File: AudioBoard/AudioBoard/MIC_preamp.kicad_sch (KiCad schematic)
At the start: 31 parts, among them SW1 SW_SPDT, U2 NE5532, U3 NE5532

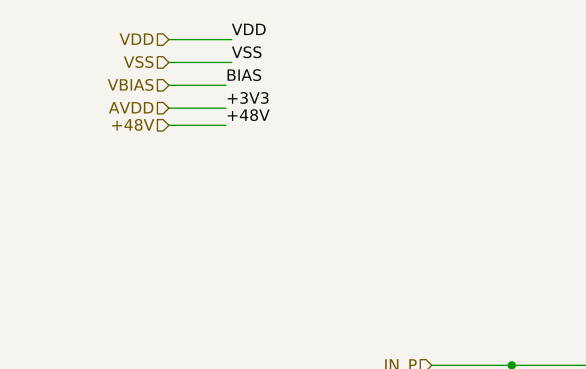
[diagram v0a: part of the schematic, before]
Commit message: added xlr output stage
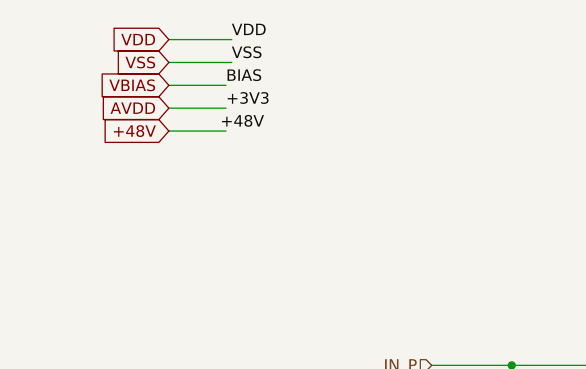
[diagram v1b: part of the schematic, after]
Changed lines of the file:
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@@
 	(wire
 		(pts
-			(xy 39.37 27.305) (xy 45.72 27.305)
+			(xy 39.37 27.94) (xy 45.72 27.94)
 		)
 		(stroke
@@
 	)
 	(label "+48V"
-		(at 45.72 27.305 0)
+		(at 45.085 27.94 0)
 		(effects
 			(font
@@
 			)
 			(justify right bottom)
+		)
+	)
+	(global_label "AVDD"
+		(shape input)
+		(at 39.37 25.4 180)
+		(fields_autoplaced yes)
+		(effects
+			(font
+				(size 1.27 1.27)
+			)
+			(justify right)
+		)
+		(property "Intersheetrefs" "${INTERSHEET_REFS}"
+			(at 31.6676 25.4 0)
+			(hide yes)
+			(show_name no)
+			(do_not_autoplace no)
+			(effects
+				(font
+					(size 1.27 1.27)
+				)
+				(justify right)
+			)
+		)
+	)
+	(global_label "VSS"
+		(shape input)
+		(at 39.37 20.32 180)
+		(fields_autoplaced yes)
+		(effects
+			(font
+				(size 1.27 1.27)
+			)
+			(justify right)
+		)
+		(property "Intersheetrefs" "${INTERSHEET_REFS}"
+			(at 32.8772 20.32 0)
+			(hide yes)
+			(show_name no)
+			(do_not_autoplace no)
+			(effects
+				(font
+					(size 1.27 1.27)
+				)
+				(justify right)
+			)
+		)
+	)
+	(global_label "+48V"
+		(shape input)
+		(at 39.37 27.94 180)
+		(fields_autoplaced yes)
+		(effects
+			(font
+				(size 1.27 1.27)
+			)
+			(justify right)
+		)
+		(property "Intersheetrefs" "${INTERSHEET_REFS}"
+			(at 31.3048 27.94 0)
+			(hide yes)
+			(show_name no)
+			(do_not_autoplace no)
+			(effects
+				(font
+					(size 1.27 1.27)
+				)
+				(justify right)
+			)
+		)
+	)
+	(global_label "VBIAS"
+		(shape input)
+		(at 39.37 22.86 180)
+		(fields_autoplaced yes)
+		(effects
+			(font
+				(size 1.27 1.27)
+			)
+			(justify right)
+		)
+		(property "Intersheetrefs" "${INTERSHEET_REFS}"
+			(at 31.1233 22.86 0)
+			(hide yes)
+			(show_name no)
+			(do_not_autoplace no)
+			(effects
+				(font
+					(size 1.27 1.27)
+				)
+				(justify right)
+			)
+		)
+	)
+	(global_label "VDD"
+		(shape input)
+		(at 39.37 17.78 180)
+		(fields_autoplaced yes)
+		(effects
+			(font
+				(size 1.27 1.27)
+			)
+			(justify right)
+		)
+		(property "Intersheetrefs" "${INTERSHEET_REFS}"
+			(at 32.7562 17.78 0)
+			(hide yes)
+			(show_name no)
+			(do_not_autoplace no)
+			(effects
+				(font
+					(size 1.27 1.27)
+				)
+				(justify right)
+			)
 		)
 	)
@@
 		)
 	)
-	(hierarchical_label "VSS"
-		(shape input)
-		(at 39.37 20.32 180)
-		(effects
-			(font
-				(size 1.27 1.27)
-			)
-			(justify right)
-		)
-	)
-	(hierarchical_label "VBIAS"
-		(shape input)
-		(at 39.37 22.86 180)
-		(effects
-			(font
-				(size 1.27 1.27)
-			)
-			(justify right)
-		)
-	)
-	(hierarchical_label "AVDD"
-		(shape input)
-		(at 39.37 25.4 180)
-		(effects
-			(font
-				(size 1.27 1.27)
-			)
-			(justify right)
-		)
-	)
-	(hierarchical_label "VDD"
-		(shape input)
-		(at 39.37 17.78 180)
-		(effects
-			(font
-				(size 1.27 1.27)
-			)
-			(justify right)
-		)
-	)
 	(hierarchical_label "OUT_P"
 		(shape output)
@@
 		)
 	)
-	(hierarchical_label "+48V"
-		(shape input)
-		(at 39.37 27.305 180)
-		(effects
-			(font
-				(size 1.27 1.27)
-			)
-			(justify right)
-		)
-	)

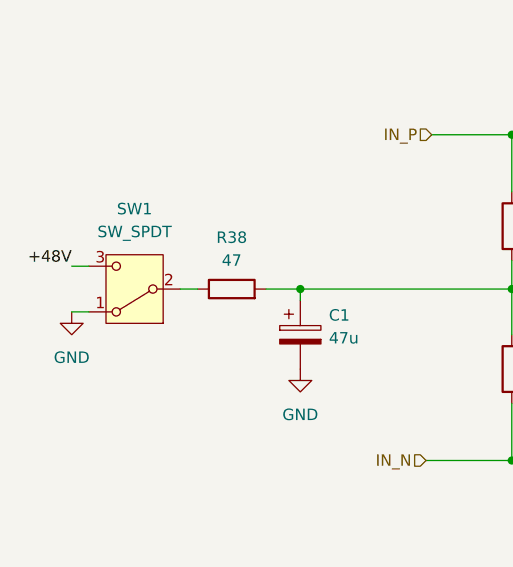
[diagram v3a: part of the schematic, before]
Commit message: added lcscpart to components and assigned footprints
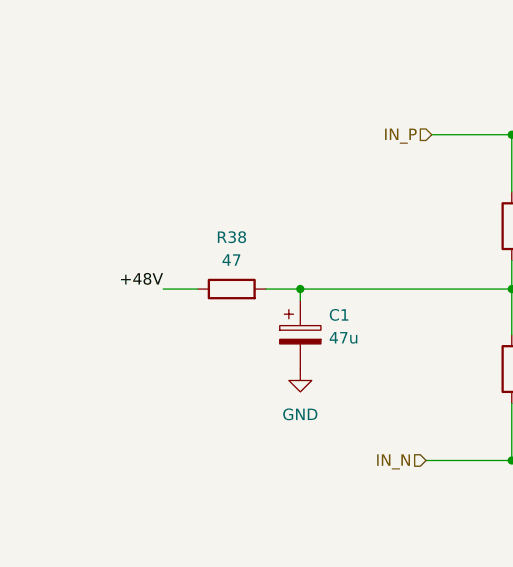
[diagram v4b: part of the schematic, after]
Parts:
- removed SW1: SW_SPDT, symbol Switch:SW_SPDT
- 100R5, 100R6: JLCPCB (none) -> C11702; LCSC Part (none) -> C11702
- C1, C40, C46: footprint (none) -> Capacitor_THT:CP_Radial_D6.3mm_P2.50mm; JLCPCB (none) -> C45673; LCSC Part (none) -> C45673
- C35, C36, C48, C49: JLCPCB (none) -> C1591; LCSC Part (none) -> C1591
- C43, C44: JLCPCB (none) -> C1523; LCSC Part (none) -> C1523
- C45, C47, C50, C51: JLCPCB (none) -> C1546; LCSC Part (none) -> C1546
- D13, D14, D15, D16: JLCPCB (none) -> C81598; LCSC Part (none) -> C81598
- R36, R37: JLCPCB (none) -> C25076; LCSC Part (none) -> C25076
- R38: footprint Resistor_SMD:R_0402_1005Metric -> Resistor_SMD:R_0603_1608Metric; JLCPCB (none) -> C23182; LCSC Part (none) -> C23182
- R39, R40, R41, R42: JLCPCB (none) -> C25879; LCSC Part (none) -> C25879
- R8, R9: footprint Resistor_SMD:R_0402_1005Metric -> Resistor_SMD:R_0603_1608Metric; JLCPCB (none) -> C23253; LCSC Part (none) -> C23253
- U2, U3: footprint (none) -> Package_SO:SOIC-8_3.9x4.9mm_P1.27mm; JLCPCB (none) -> C7426; LCSC Part (none) -> C7426
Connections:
- net +48V: now also R38.1
